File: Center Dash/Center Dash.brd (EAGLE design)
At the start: 159 x 86.7 mm, 55 parts, among them J1 502585-0470, U2 TPS54540DDARQ1

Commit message: Fixed Ashers fuck up
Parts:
- added R3, R5, R9: 100, rcl:R0805
- C1, C11, C13, C14, C15, C16, C2, C3, C4, C5, C6, C7: value (none) -> 10uF; device rcl:C0402 -> rcl:C0603K
- moved C16 134.2 mm to (64.5, 80.5)
- moved C13 39.3 mm to (29.1, 97.4)
- moved C2 14.0 mm to (-58.4, 87.2)
- moved C5 12.9 mm to (-21.8, 99.9)
- moved C1 12.9 mm to (-69.5, 80.5)
- moved C7 12.8 mm to (3.94, 101.5)
- moved C6 12.7 mm to (-8.89, 101.3)
- moved C11 12.5 mm to (16.8, 99.9)
- moved C3 12.3 mm to (-45.8, 93.3)
- moved C4 12.2 mm to (-33.9, 97.4)
- moved C15 0.18 mm to (53.6, 87.2)
- moved C14 0.05 mm to (40.9, 93.5)
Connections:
- removed net SPARE_4: U$1.P$7, U$2.36/A17
- removed net SPARE_5: U$1.P$6, U$2.37/A18
- new net IGNITION_1: R5.2, U$1.P$12, U$2.33/A14
- new net IGNITION_2: R3.2, U$1.P$11, U$2.34/A15
- new net N$11: LED1.4-DIN, R9.1
- net +3V3: now also R3.1, R5.1
- net DI1: now also R9.2; no longer LED1.4-DIN
- net SPARE_1: now also U$1.P$8, U$2.35/A16; no longer U$1.P$12, U$2.33/A14
- net SPARE_2: now also U$1.P$7, U$2.36/A17; no longer U$1.P$11, U$2.34/A15
- net SPARE_3: now also U$1.P$6, U$2.37/A18; no longer U$1.P$8, U$2.35/A16
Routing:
- net IGNITION_1: track 0.00 -> 66.4 mm, vias 0 -> 4
- net N$11: track 0.00 -> 65.2 mm, vias 0 -> 1
- net DI1: track 93.9 -> 30.5 mm, vias 2 -> 1
- net IGNITION_2: track 0.00 -> 62.1 mm, vias 0 -> 4
- net SPARE_4: track 55.8 -> 0.00 mm, vias 2 -> 0
- net SPARE_5: track 49.0 -> 0.00 mm, vias 2 -> 0
- net SPARE_1: track 46.3 -> 63.6 mm
- net SPARE_2: track 39.9 -> 55.8 mm
- net SPARE_3: track 63.6 -> 49.0 mm
- net +3V3: track 78.8 -> 84.2 mm, vias 1 -> 2
- net CAN_RX: track 85.3 -> 86.2 mm

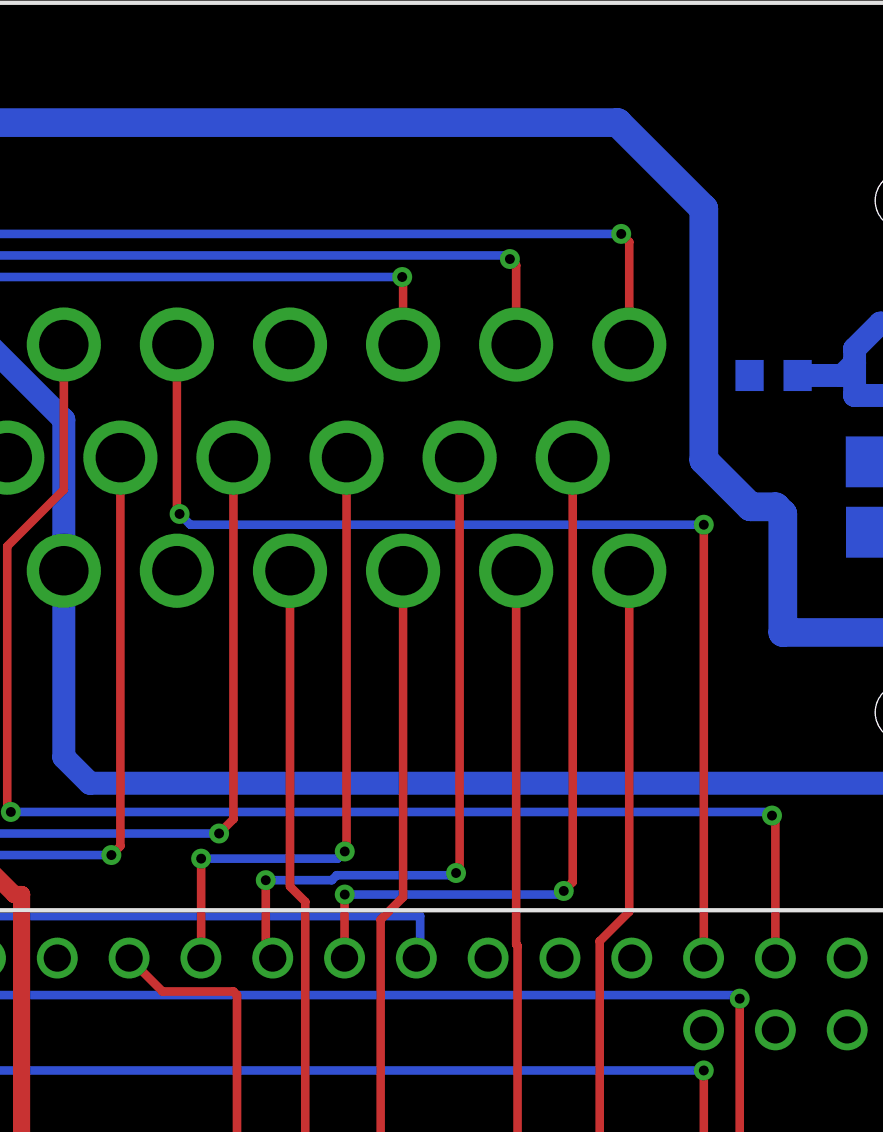
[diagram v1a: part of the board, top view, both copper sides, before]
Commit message: Made changes
Change LED caps to .1uF on right ear and center
Add resistor to D2
Add level shifters (1 for D1, 1 for D2)
Add mount holes on right ear
Add mosfet for servo (see things to consider.txt)
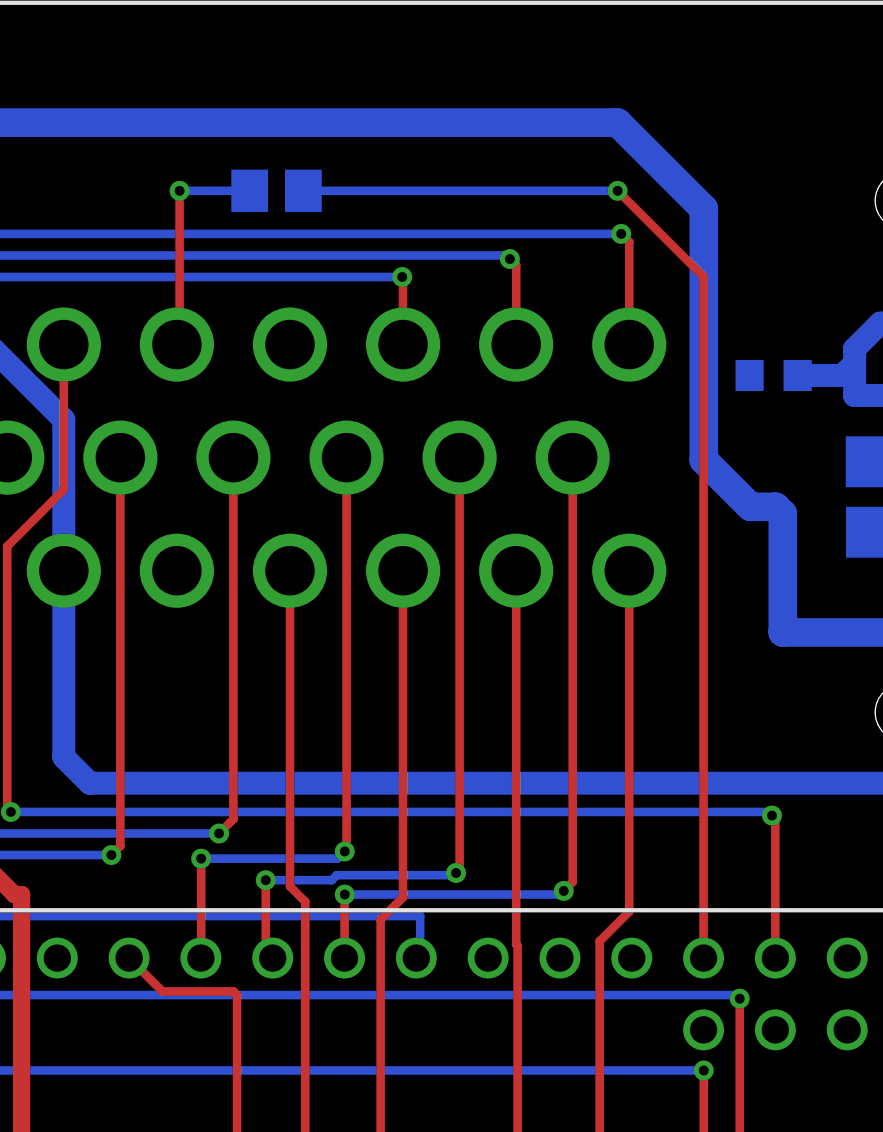
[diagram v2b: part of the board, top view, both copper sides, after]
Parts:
- added R11: 100, rcl:R0805
- C1, C11, C13, C14, C15, C16, C2, C3, C4, C5, C6, C7: value 10uF -> .1uF
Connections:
- new net DI2_MORE: R11.1, U$1.P$4
- net DI2: now also R11.2; no longer U$1.P$4
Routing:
- net DI2_MORE: track 0.00 -> 7.96 mm, vias 0 -> 1
- net DI2: track 40.1 -> 39.5 mm, vias 2 -> 1
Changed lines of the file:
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@@
 <?xml version="1.0" encoding="utf-8"?>
 <!DOCTYPE eagle SYSTEM "eagle.dtd">
-<eagle version="8.5.0">
+<eagle version="8.3.1">
 <drawing>
 <settings>
@@
 <param name="dpMaxLengthDifference" value="10mm"/>
 <param name="dpGapFactor" value="2.5"/>
+<param name="checkGrid" value="0"/>
 <param name="checkAngle" value="0"/>
 <param name="checkFont" value="1"/>
 <param name="checkRestrict" value="1"/>
-<param name="checkStop" value="0"/>
-<param name="checkValues" value="0"/>
 <param name="useDiameter" value="13"/>
 <param name="maxErrors" value="50"/>
@@
 <attribute name="NAME" x="35.56" y="56.642" size="1.27" layer="25" rot="R270"/>
 </element>
-<element name="C1" library="rcl" package="C0603K" value="10uF" x="-69.469" y="80.518" smashed="yes" rot="R270">
+<element name="C1" library="rcl" package="C0603K" value=".1uF" x="-69.469" y="80.518" smashed="yes" rot="R270">
 <attribute name="NAME" x="-68.819" y="81.318" size="1.016" layer="25" rot="R270"/>
 <attribute name="PARTNO" value="GRM188R61A106KE69D" x="-69.469" y="80.518" size="1.778" layer="27" rot="R270" display="off"/>
 </element>
-<element name="C2" library="rcl" package="C0603K" value="10uF" x="-58.42" y="87.249" smashed="yes" rot="R270">
+<element name="C2" library="rcl" package="C0603K" value=".1uF" x="-58.42" y="87.249" smashed="yes" rot="R270">
 <attribute name="NAME" x="-57.77" y="88.049" size="1.016" layer="25" rot="R270"/>
 <attribute name="PARTNO" value="GRM188R61A106KE69D" x="-58.42" y="87.249" size="1.778" layer="27" rot="R270" display="off"/>
 </element>
-<element name="C3" library="rcl" package="C0603K" value="10uF" x="-45.847" y="93.345" smashed="yes" rot="R270">
+<element name="C3" library="rcl" package="C0603K" value=".1uF" x="-45.847" y="93.345" smashed="yes" rot="R270">
 <attribute name="NAME" x="-45.197" y="94.145" size="1.016" layer="25" rot="R270"/>
 <attribute name="PARTNO" value="GRM188R61A106KE69D" x="-45.847" y="93.345" size="1.778" layer="27" rot="R270" display="off"/>
 </element>
-<element name="C4" library="rcl" package="C0603K" value="10uF" x="-33.909" y="97.409" smashed="yes" rot="R270">
+<element name="C4" library="rcl" package="C0603K" value=".1uF" x="-33.909" y="97.409" smashed="yes" rot="R270">
 <attribute name="NAME" x="-33.259" y="98.209" size="1.016" layer="25" rot="R270"/>
 <attribute name="PARTNO" value="GRM188R61A106KE69D" x="-33.909" y="97.409" size="1.778" layer="27" rot="R270" display="off"/>
 </element>
-<element name="C5" library="rcl" package="C0603K" value="10uF" x="-21.844" y="99.949" smashed="yes" rot="R270">
+<element name="C5" library="rcl" package="C0603K" value=".1uF" x="-21.844" y="99.949" smashed="yes" rot="R270">
 <attribute name="NAME" x="-21.194" y="100.749" size="1.016" layer="25" rot="R270"/>
 <attribute name="PARTNO" value="GRM188R61A106KE69D" x="-21.844" y="99.949" size="1.778" layer="27" rot="R270" display="off"/>
 </element>
-<element name="C6" library="rcl" package="C0603K" value="10uF" x="-8.89" y="101.346" smashed="yes" rot="R270">
+<element name="C6" library="rcl" package="C0603K" value=".1uF" x="-8.89" y="101.346" smashed="yes" rot="R270">
 <attribute name="NAME" x="-8.24" y="102.146" size="1.016" layer="25" rot="R270"/>
 <attribute name="PARTNO" value="GRM188R61A106KE69D" x="-8.89" y="101.346" size="1.778" layer="27" rot="R270" display="off"/>
 </element>
-<element name="C7" library="rcl" package="C0603K" value="10uF" x="3.937" y="101.473" smashed="yes" rot="R270">
+<element name="C7" library="rcl" package="C0603K" value=".1uF" x="3.937" y="101.473" smashed="yes" rot="R270">
 <attribute name="NAME" x="4.587" y="102.273" size="1.016" layer="25" rot="R270"/>
 <attribute name="PARTNO" value="GRM188R61A106KE69D" x="3.937" y="101.473" size="1.778" layer="27" rot="R270" display="off"/>
 </element>
-<element name="C11" library="rcl" package="C0603K" value="10uF" x="16.764" y="99.949" smashed="yes" rot="R270">
+<element name="C11" library="rcl" package="C0603K" value=".1uF" x="16.764" y="99.949" smashed="yes" rot="R270">
 <attribute name="NAME" x="17.414" y="100.749" size="1.016" layer="25" rot="R270"/>
 <attribute name="PARTNO" value="GRM188R61A106KE69D" x="16.764" y="99.949" size="1.778" layer="27" rot="R270" display="off"/>
 </element>
-<element name="C13" library="rcl" package="C0603K" value="10uF" x="29.083" y="97.409" smashed="yes" rot="R270">
+<element name="C13" library="rcl" package="C0603K" value=".1uF" x="29.083" y="97.409" smashed="yes" rot="R270">
 <attribute name="NAME" x="29.733" y="98.209" size="1.016" layer="25" rot="R270"/>
 <attribute name="PARTNO" value="GRM188R61A106KE69D" x="29.083" y="97.409" size="1.778" layer="27" rot="R270" display="off"/>
 </element>
-<element name="C14" library="rcl" package="C0603K" value="10uF" x="40.894" y="93.472" smashed="yes" rot="R270">
+<element name="C14" library="rcl" package="C0603K" value=".1uF" x="40.894" y="93.472" smashed="yes" rot="R270">
 <attribute name="NAME" x="41.544" y="94.272" size="1.016" layer="25" rot="R270"/>
 <attribute name="PARTNO" value="GRM188R61A106KE69D" x="40.894" y="93.472" size="1.778" layer="27" rot="R270" display="off"/>
 </element>
-<element name="C15" library="rcl" package="C0603K" value="10uF" x="53.594" y="87.249" smashed="yes" rot="R270">
+<element name="C15" library="rcl" package="C0603K" value=".1uF" x="53.594" y="87.249" smashed="yes" rot="R270">
 <attribute name="NAME" x="54.244" y="88.049" size="1.016" layer="25" rot="R270"/>
 <attribute name="PARTNO" value="GRM188R61A106KE69D" x="53.594" y="87.249" size="1.778" layer="27" rot="R270" display="off"/>
 </element>
-<element name="C16" library="rcl" package="C0603K" value="10uF" x="64.516" y="80.518" smashed="yes" rot="R270">
+<element name="C16" library="rcl" package="C0603K" value=".1uF" x="64.516" y="80.518" smashed="yes" rot="R270">
 <attribute name="NAME" x="65.166" y="81.318" size="1.016" layer="25" rot="R270"/>
 <attribute name="PARTNO" value="GRM188R61A106KE69D" x="64.516" y="80.518" size="1.778" layer="27" rot="R270" display="off"/>
+</element>
+<element name="R11" library="rcl" package="R0805" value="100" x="1.524" y="79.375" smashed="yes" rot="MR180">
+<attribute name="NAME" x="-3.81" y="80.01" size="1.27" layer="26" rot="MR180"/>
 </element>
 </elements>
@@
 </signal>
 <signal name="DI2">
-<contactref element="U$1" pad="P$4"/>
 <contactref element="U$2" pad="21/A7"/>
-<wire x1="-2" y1="73.937" x2="-2" y2="68.04" width="0.3048" layer="1"/>
-<wire x1="-2" y1="68.04" x2="-1.905" y2="67.945" width="0.3048" layer="1"/>
-<via x="-1.905" y="67.945" extent="1-16" drill="0.35"/>
-<wire x1="-1.905" y1="67.945" x2="-1.524" y2="67.564" width="0.3048" layer="16"/>
-<wire x1="-1.524" y1="67.564" x2="16.637" y2="67.564" width="0.3048" layer="16"/>
-<via x="16.637" y="67.564" extent="1-16" drill="0.35"/>
-<wire x1="16.637" y1="67.564" x2="16.637" y2="52.244" width="0.3048" layer="1"/>
-<wire x1="16.637" y1="52.244" x2="16.629" y2="52.236" width="0.3048" layer="1"/>
+<contactref element="R11" pad="2"/>
+<wire x1="16.629" y1="52.236" x2="16.629" y2="76.335" width="0.3048" layer="1"/>
+<wire x1="16.629" y1="76.335" x2="13.589" y2="79.375" width="0.3048" layer="1"/>
+<via x="13.589" y="79.375" extent="1-16" drill="0.35"/>
+<wire x1="13.589" y1="79.375" x2="2.474" y2="79.375" width="0.3048" layer="16"/>
 </signal>
 <signal name="N$2">
@@
 <wire x1="62.23" y1="81.28" x2="62.865" y2="80.645" width="0.3048" layer="16"/>
 </signal>
+<signal name="DI2_MORE">
+<contactref element="R11" pad="1"/>
+<contactref element="U$1" pad="P$4"/>
+<wire x1="0.574" y1="79.375" x2="-1.905" y2="79.375" width="0.3048" layer="16"/>
+<via x="-1.905" y="79.375" extent="1-16" drill="0.35"/>
+<wire x1="-1.905" y1="79.375" x2="-1.905" y2="74.032" width="0.3048" layer="1"/>
+<wire x1="-1.905" y1="74.032" x2="-2" y2="73.937" width="0.3048" layer="1"/>
+</signal>
 </signals>

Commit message: Redid right ear board layouts
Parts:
- moved H2 3.95 mm to (2.67, 27.6), turned to 0 degrees
- moved H3 3.95 mm to (-16.4, 27.6), turned to 0 degrees
- moved JP2 2.92 mm to (14.5, 27.8)
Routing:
- net N$26: track 34.2 -> 45.1 mm, vias 1 -> 3
- net N$19: track 32.9 -> 43.0 mm, vias 1 -> 3
- net N$18: track 32.7 -> 42.1 mm, vias 1 -> 3
- net +5V: track 368.9 -> 359.5 mm
- net MOSI: track 14.4 -> 7.09 mm, vias 1 -> 0
- net N$17: track 32.7 -> 39.6 mm, vias 1 -> 3
- net N$16: track 32.5 -> 38.0 mm, vias 1 -> 3
- net MISO: track 15.9 -> 11.0 mm
- net CS: track 12.3 -> 7.66 mm, vias 1 -> 2
- net +15V: track 88.3 -> 84.9 mm
- net N$27: track 16.7 -> 13.3 mm
- net N$15: track 32.6 -> 35.3 mm, vias 1 -> 3
- net CLK: track 28.5 -> 26.0 mm
- net N$3: track 31.3 -> 30.8 mm, vias 1 -> 2
- net N$13: track 32.4 -> 32.9 mm, vias 1 -> 2
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
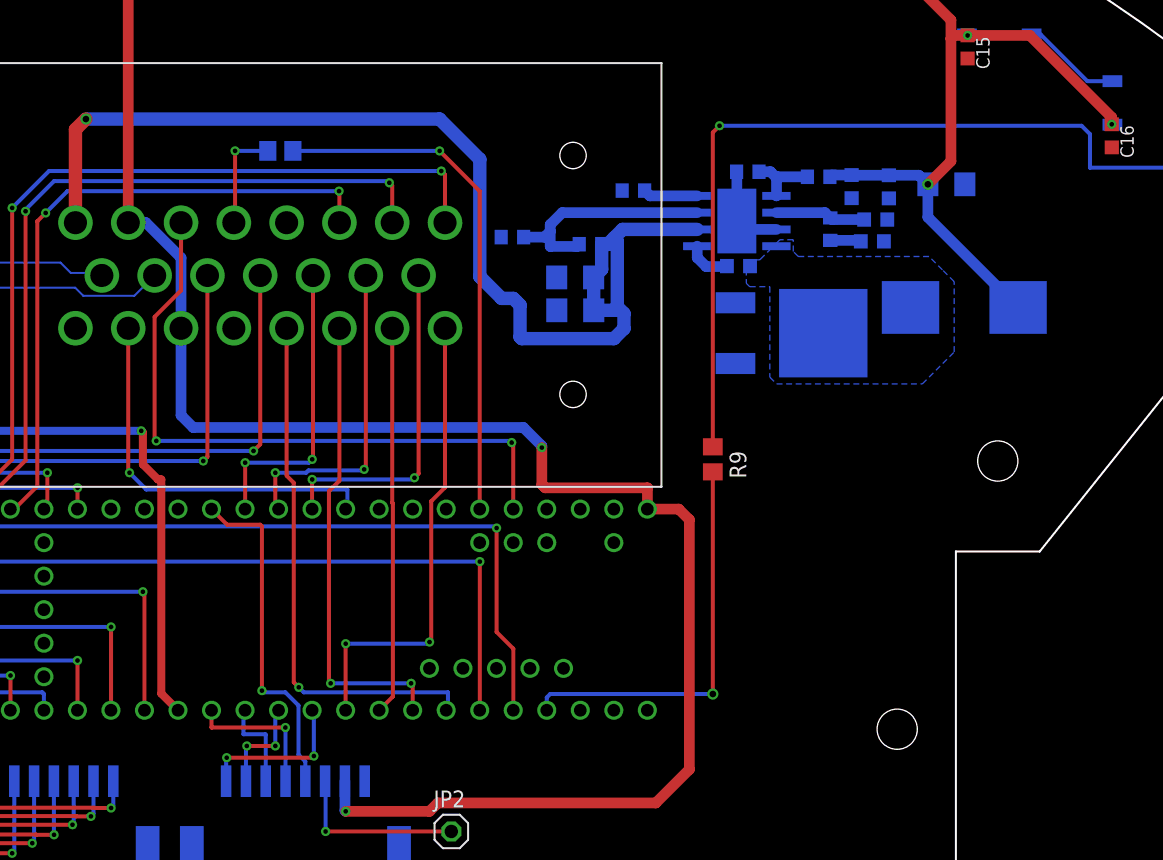
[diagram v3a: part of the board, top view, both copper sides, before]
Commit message: Added level shifter to center dash
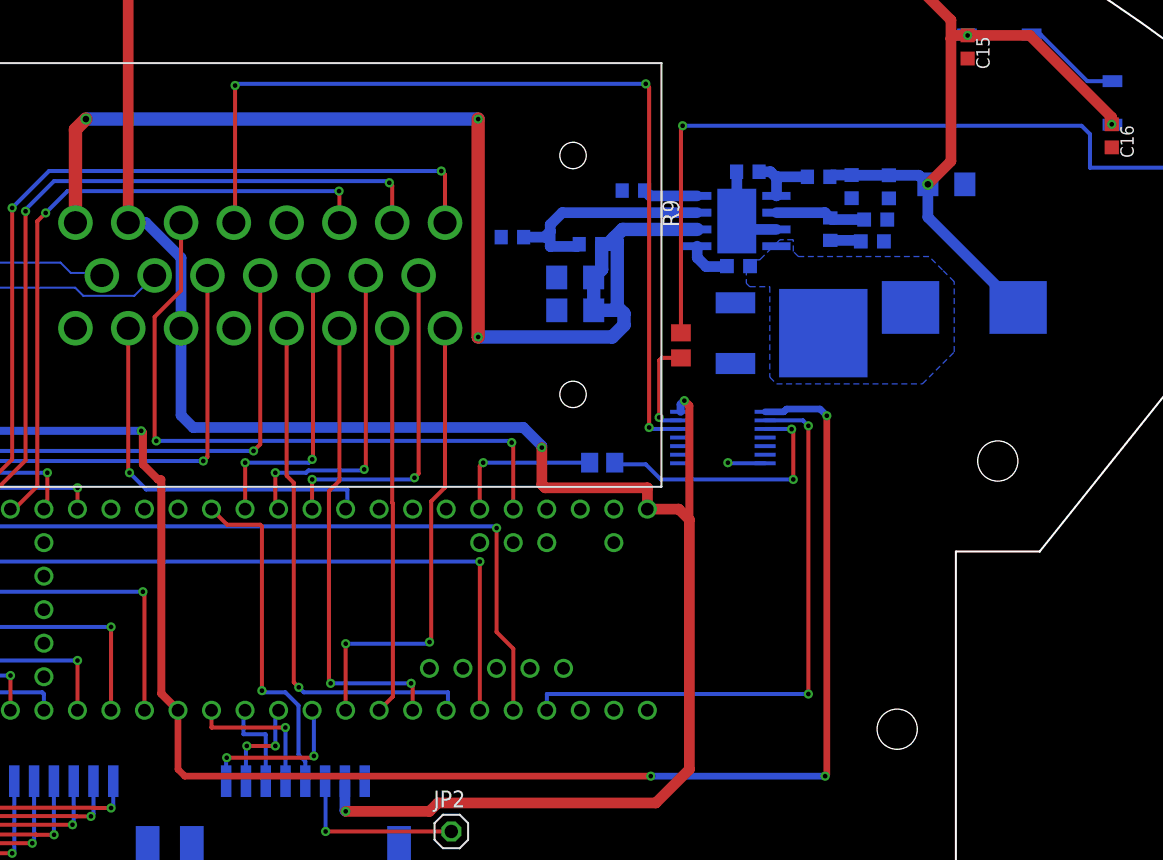
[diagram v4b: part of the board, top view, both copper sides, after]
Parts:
- added U1: ADG3304BRUZ-REEL7, FormE:ADG3304
- moved R11 33.9 mm to (25.9, 55.8), turned to 0 degrees
- moved R9 8.97 mm to (31.9, 64.6)
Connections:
- removed net DI1: R9.2, U$2.2
- new net DI: U$2.2, U1.2
- new net DI_MORE: R11.1, U1.3
- new net N$21: R9.2, U1.13
- net +3V3: now also U1.1
- net +5V: now also U1.14
- net DI2_MORE: now also U1.12; no longer R11.1
- net GND: now also U1.7
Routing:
- net +3V3: track 84.2 -> 170.3 mm, vias 2 -> 5
- net DI2_MORE: track 7.96 -> 70.2 mm, vias 1 -> 3
- net DI: track 0.00 -> 44.8 mm, vias 0 -> 2
- net DI1: track 30.5 -> 0.00 mm, vias 1 -> 0
- net DI2: track 39.5 -> 11.7 mm
- net DI_MORE: track 0.00 -> 19.9 mm, vias 0 -> 2
- net +5V: track 359.5 -> 369.6 mm, vias 16 -> 17
- net N$21: track 0.00 -> 7.77 mm, vias 0 -> 1
- net N$11: track 65.2 -> 59.2 mm
- net GND: track 10.1 -> 13.1 mm, vias 0 -> 1
- net +15V: track 84.9 -> 87.7 mm, vias 1 -> 3

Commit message: Done with board layouts
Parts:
- added JP3, JP4, JP7: (no value), pinhead:1X01
- added JP5, JP6, JP8: (no value), pinhead:1X02
- added LED13, LED14, LED15: GREEN, FormE:CHIP-LED0805
- added R12: 0/DNP, rcl:R0805
- added R13, R14, R15: 1K, adafruit:R0805
- moved R11 28.8 mm to (23.2, 84.5), turned to 180 degrees
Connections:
- removed net DI2: R11.2, U$2.21/A7
- new net DI2_OUT: R11.1, U$1.P$4
- new net N$20: LED14.C, R14.2
- new net N$22: LED15.C, R15.2
- new net N$56: LED13.C, R13.2
- net +15V: now also LED15.A
- net +3V3: now also LED13.A
- net +5V: now also LED14.A
- net CAN_RX: now also JP6.1
- net CAN_TX: now also JP6.2
- net DI2_MORE: now also JP5.2, R11.2; no longer U$1.P$4
- net DI_MORE: now also U$2.21/A7; no longer R11.1
- net GND: now also JP3.1, JP4.1, R13.1, R14.1, R15.1
- net MISO: now also JP8.1
- net MOSI: now also JP8.2
- net N$11: now also R12.1
- net N$2: now also R12.2
- net N$21: now also JP5.1
- net SERVO_PWM: now also JP7.1
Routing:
- net DI2_OUT: track 0.00 -> 34.6 mm, vias 0 -> 1
- net MOSI: track 7.09 -> 38.9 mm, vias 0 -> 1
- net CAN_RX: track 86.2 -> 115.7 mm, vias 3 -> 5
- net +15V: track 87.7 -> 115.7 mm
- net DI2_MORE: track 70.2 -> 43.8 mm
- net N$2: track 7.59 -> 33.8 mm
- net MISO: track 11.0 -> 36.1 mm, vias 1 -> 2
- net CAN_TX: track 80.1 -> 104.2 mm
- net GND: track 13.1 -> 32.8 mm, vias 1 -> 5
- net SERVO_PWM: track 49.5 -> 67.5 mm
- net +5V: track 369.6 -> 384.4 mm, vias 17 -> 19
- net N$21: track 7.77 -> 21.7 mm, vias 1 -> 2
- net DI_MORE: track 19.9 -> 33.4 mm, vias 2 -> 3
- net DI2: track 11.7 -> 0.00 mm, vias 1 -> 0
- net +3V3: track 170.3 -> 172.4 mm
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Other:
- board text added: "3v3"
- board text added: "5v"
- board text added: "CAN_RX"
- board text added: "CAN_TX"
- board text added: "DI"
- board text added: "DI2"
- board text added: "Free Pin"
- board text added: "Free Pins"
- board text added: "GND"
- board text added: "MISO"
- board text added: "MOSI"
- board text added: "PWM"
- board text added: "VCC"
